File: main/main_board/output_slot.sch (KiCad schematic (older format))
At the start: 6 parts, among them M1 microzed, P1 my_pcie_8x

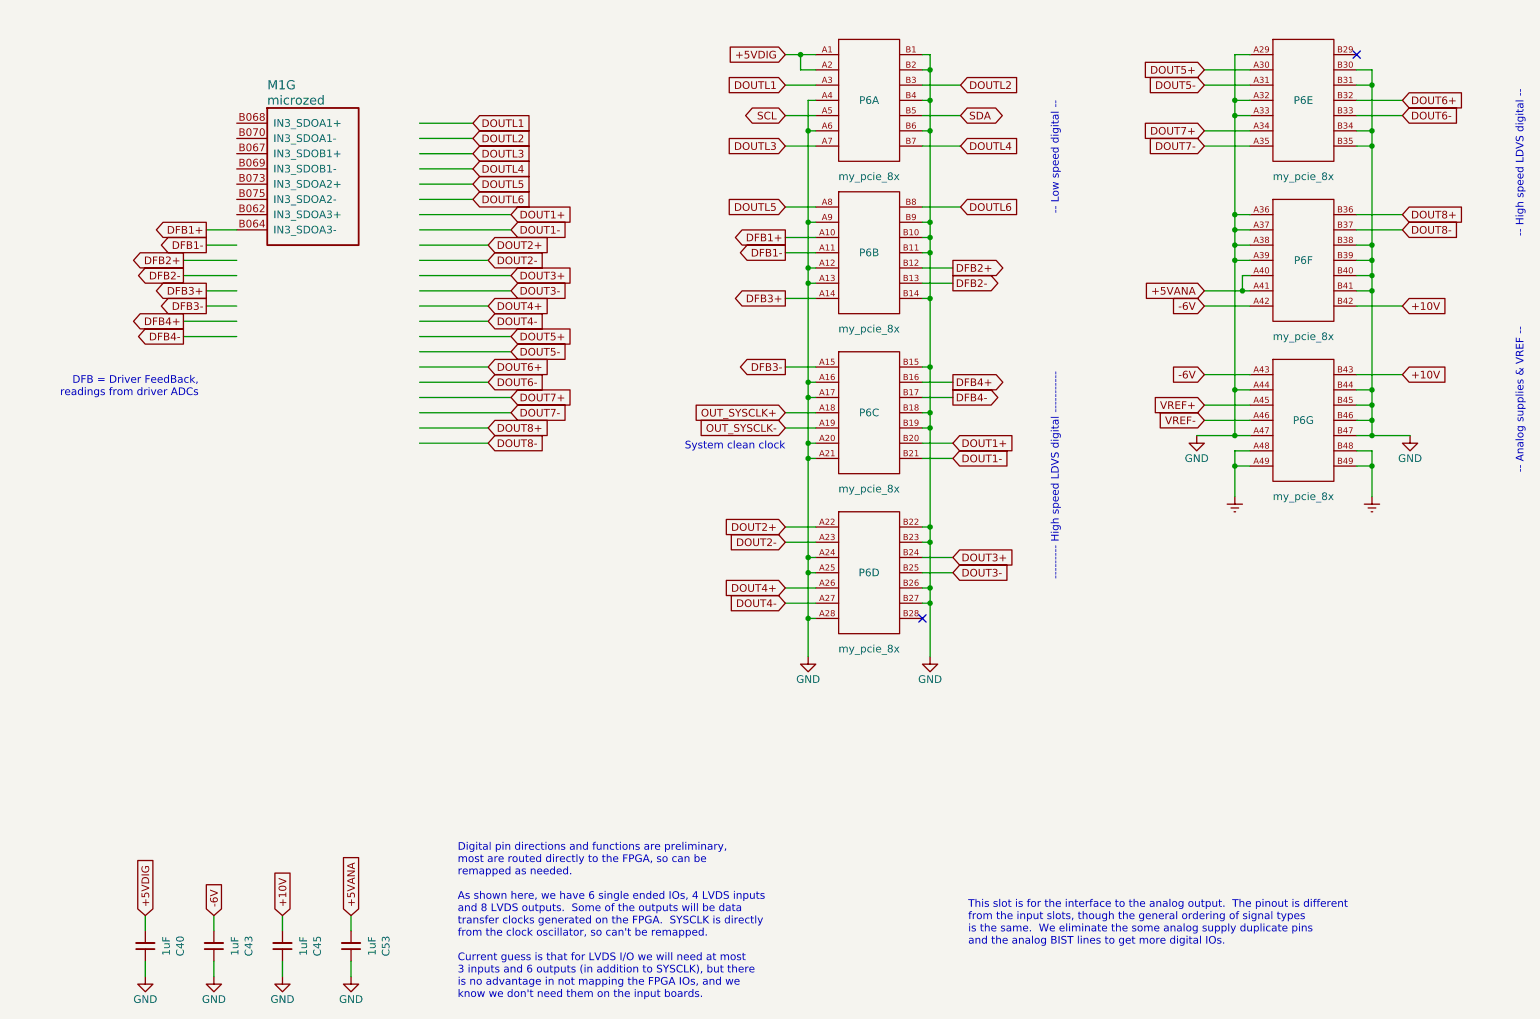
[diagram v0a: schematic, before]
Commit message: Various preparations for routing the main board. Cleaned up the BOM and reconciled it with the Digikey BOM, so lots of component attributes have changed. This involved pinning down some components which had been vague, especially ferrite beads and chip capacitors. 1uF capacitors have all been changed to 10uF. Changed CARDSEL lines to be buffered rather than filtered, since we had the unused buffers sitting there. Another pass on the Microzed pin mapping.  Brought out the DEBUG LVDS line, and tweaked orderings. Added RC filter and pullups on I2C and PROBE_CONFIG.  We might need level translators here to get >=3.3V Added mount holes for the low volt regulator daughtercard, and dimensioned the connector location.
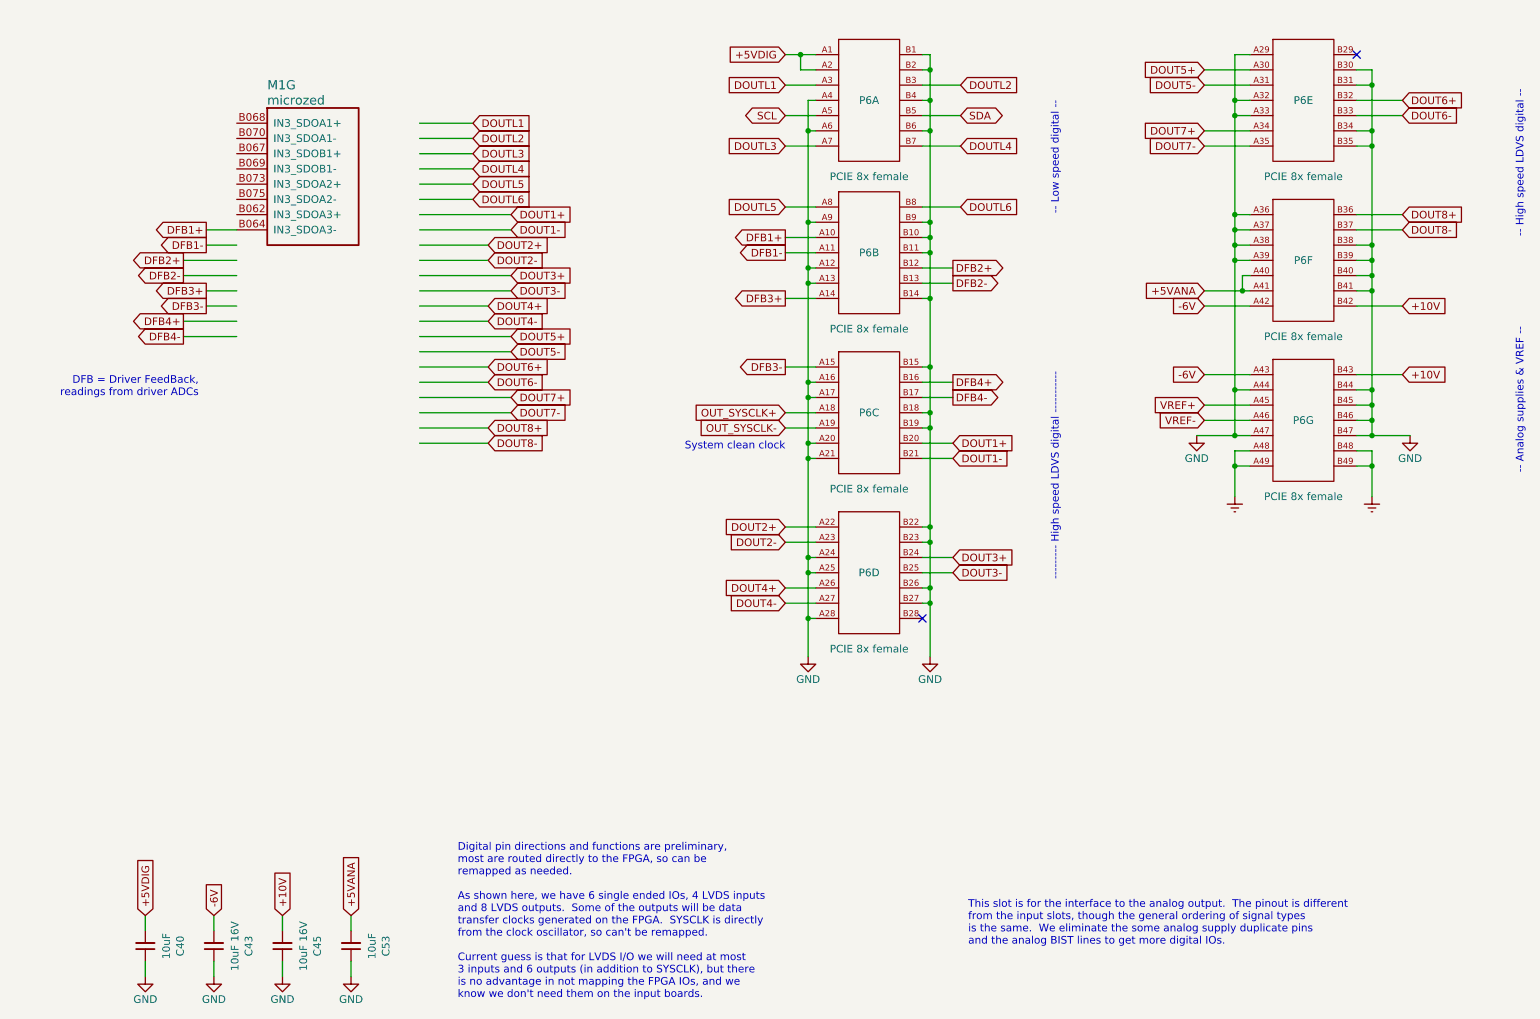
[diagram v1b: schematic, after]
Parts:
- C40, C53: value 1uF -> 10uF; footprint Capacitor_SMD:C_0805_2012Metric -> Capacitor_SMD:C_0603_1608Metric; DK line 27 -> 20; Description CAP CER 1UF 16V X7R 0805 -> CAP CER 10UF 6.3V X5R 0603; Digikey 1276-6471-1-ND -> 478-5318-1-ND; MPN CL21B105KOFNNNG -> 06036D106MAT2A; Manufacturer (none) -> AVX
- C43, C45: value 1uF -> 10uF 16V; DK line 27 -> 10; Description CAP CER 1UF 16V X7R 0805 -> CAP CER 10UF 16V X5R 0805; Digikey 1276-6471-1-ND -> 399-8012-1-ND; MPN CL21B105KOFNNNG -> C0805C106K4PACTU; Manufacturer (none) -> KEMET
- P1: value my_pcie_8x -> PCIE 8x female; DK line (none) -> 2; Description (none) -> CONN PCI EXP FEMALE 98POS 0.039; Digikey (none) -> 609-1970-ND; MPN (none) -> 10018783-10102TLF; Manufacturer (none) -> Amphenol ICC (FCI)
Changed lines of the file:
@@
 AR Path="/5EC15224/5EC152AD" Ref="P6"  Part="3"
 F 0 "P6" H 6450 3450 50  0000 C CNN
-F 1 "my_pcie_8x" H 6450 2950 50  0000 C CNN
+F 1 "PCIE 8x female" H 6450 2950 50  0000 C CNN
 F 2 "input:PCIE_8x_female" H 6450 3950 50  0001 C CNN
-F 3 "" H 6450 3450 50  0001 C CNN
+F 3 "https://www.amphenol-icc.com/media/wysiwyg/files/drawing/10018783.pdf" H 6450 3450 50  0001 C CNN
+F 4 "CONN PCI EXP FEMALE 98POS 0.039" H 6450 3450 50  0001 C CNN "Description"
+F 5 "609-1970-ND" H 6450 3450 50  0001 C CNN "Digikey"
+F 6 "10018783-10102TLF" H 6450 3450 50  0001 C CNN "MPN"
+F 7 "Amphenol ICC (FCI)" H 6450 3450 50  0001 C CNN "Manufacturer"
+F 8 "2" H 6450 3450 50  0001 C CNN "DK line"
 	3    6450 3450
 	1    0    0    -1
@@
 AR Path="/5EC15224/5EC152AF" Ref="P6"  Part="5"
 F 0 "P6" H 9300 1400 50  0000 C CNN
-F 1 "my_pcie_8x" H 9300 900 50  0000 C CNN
+F 1 "PCIE 8x female" H 9300 900 50  0000 C CNN
 F 2 "input:PCIE_8x_female" H 9300 1900 50  0001 C CNN
-F 3 "" H 9300 1400 50  0001 C CNN
+F 3 "https://www.amphenol-icc.com/media/wysiwyg/files/drawing/10018783.pdf" H 9300 1400 50  0001 C CNN
+F 4 "CONN PCI EXP FEMALE 98POS 0.039" H 9300 1400 50  0001 C CNN "Description"
+F 5 "609-1970-ND" H 9300 1400 50  0001 C CNN "Digikey"
+F 6 "10018783-10102TLF" H 9300 1400 50  0001 C CNN "MPN"
+F 7 "Amphenol ICC (FCI)" H 9300 1400 50  0001 C CNN "Manufacturer"
+F 8 "2" H 9300 1400 50  0001 C CNN "DK line"
 	5    9300 1400
 	1    0    0    -1
@@
 AR Path="/5EC15224/5EC152A8" Ref="P6"  Part="6"
 F 0 "P6" H 9300 2450 50  0000 C CNN
-F 1 "my_pcie_8x" H 9300 1950 50  0000 C CNN
+F 1 "PCIE 8x female" H 9300 1950 50  0000 C CNN
 F 2 "input:PCIE_8x_female" H 9300 2950 50  0001 C CNN
-F 3 "" H 9300 2450 50  0001 C CNN
+F 3 "https://www.amphenol-icc.com/media/wysiwyg/files/drawing/10018783.pdf" H 9300 2450 50  0001 C CNN
+F 4 "CONN PCI EXP FEMALE 98POS 0.039" H 9300 2450 50  0001 C CNN "Description"
+F 5 "609-1970-ND" H 9300 2450 50  0001 C CNN "Digikey"
+F 6 "10018783-10102TLF" H 9300 2450 50  0001 C CNN "MPN"
+F 7 "Amphenol ICC (FCI)" H 9300 2450 50  0001 C CNN "Manufacturer"
+F 8 "2" H 9300 2450 50  0001 C CNN "DK line"
 	6    9300 2450
 	1    0    0    -1
@@
 AR Path="/5EC15224/5EC152A9" Ref="P6"  Part="7"
 F 0 "P6" H 9300 3500 50  0000 C CNN
-F 1 "my_pcie_8x" H 9300 3000 50  0000 C CNN
+F 1 "PCIE 8x female" H 9300 3000 50  0000 C CNN
 F 2 "input:PCIE_8x_female" H 9300 4000 50  0001 C CNN
-F 3 "" H 9300 3500 50  0001 C CNN
+F 3 "https://www.amphenol-icc.com/media/wysiwyg/files/drawing/10018783.pdf" H 9300 3500 50  0001 C CNN
+F 4 "CONN PCI EXP FEMALE 98POS 0.039" H 9300 3500 50  0001 C CNN "Description"
+F 5 "609-1970-ND" H 9300 3500 50  0001 C CNN "Digikey"
+F 6 "10018783-10102TLF" H 9300 3500 50  0001 C CNN "MPN"
+F 7 "Amphenol ICC (FCI)" H 9300 3500 50  0001 C CNN "Manufacturer"
+F 8 "2" H 9300 3500 50  0001 C CNN "DK line"
 	7    9300 3500
 	1    0    0    -1
@@
 AR Path="/5EC15224/5E625DE3" Ref="P6"  Part="2"
 F 0 "P6" H 6450 2400 50  0000 C CNN
-F 1 "my_pcie_8x" H 6450 1900 50  0000 C CNN
+F 1 "PCIE 8x female" H 6450 1900 50  0000 C CNN
 F 2 "input:PCIE_8x_female" H 6450 2900 50  0001 C CNN
-F 3 "" H 6450 2400 50  0001 C CNN
+F 3 "https://www.amphenol-icc.com/media/wysiwyg/files/drawing/10018783.pdf" H 6450 2400 50  0001 C CNN
+F 4 "CONN PCI EXP FEMALE 98POS 0.039" H 6450 2400 50  0001 C CNN "Description"
+F 5 "609-1970-ND" H 6450 2400 50  0001 C CNN "Digikey"
+F 6 "10018783-10102TLF" H 6450 2400 50  0001 C CNN "MPN"
+F 7 "Amphenol ICC (FCI)" H 6450 2400 50  0001 C CNN "Manufacturer"
+F 8 "2" H 6450 2400 50  0001 C CNN "DK line"
 	2    6450 2400
 	1    0    0    -1
@@
 AR Path="/5EC15224/5EC152AE" Ref="P6"  Part="1"
 F 0 "P6" H 6450 1400 50  0000 C CNN
-F 1 "my_pcie_8x" H 6450 900 50  0000 C CNN
+F 1 "PCIE 8x female" H 6450 900 50  0000 C CNN
 F 2 "input:PCIE_8x_female" H 6450 1900 50  0001 C CNN
-F 3 "" H 6450 1400 50  0001 C CNN
+F 3 "https://www.amphenol-icc.com/media/wysiwyg/files/drawing/10018783.pdf" H 6450 1400 50  0001 C CNN
+F 4 "CONN PCI EXP FEMALE 98POS 0.039" H 6450 1400 50  0001 C CNN "Description"
+F 5 "609-1970-ND" H 6450 1400 50  0001 C CNN "Digikey"
+F 6 "10018783-10102TLF" H 6450 1400 50  0001 C CNN "MPN"
+F 7 "Amphenol ICC (FCI)" H 6450 1400 50  0001 C CNN "Manufacturer"
+F 8 "2" H 6450 1400 50  0001 C CNN "DK line"
 	1    6450 1400
 	1    0    0    -1
@@
 AR Path="/5EC15224/5E625DE5" Ref="P6"  Part="4"
 F 0 "P6" H 6450 4500 50  0000 C CNN
-F 1 "my_pcie_8x" H 6450 4000 50  0000 C CNN
+F 1 "PCIE 8x female" H 6450 4000 50  0000 C CNN
 F 2 "input:PCIE_8x_female" H 6450 5000 50  0001 C CNN
-F 3 "" H 6450 4500 50  0001 C CNN
+F 3 "https://www.amphenol-icc.com/media/wysiwyg/files/drawing/10018783.pdf" H 6450 4500 50  0001 C CNN
+F 4 "CONN PCI EXP FEMALE 98POS 0.039" H 6450 4500 50  0001 C CNN "Description"
+F 5 "609-1970-ND" H 6450 4500 50  0001 C CNN "Digikey"
+F 6 "10018783-10102TLF" H 6450 4500 50  0001 C CNN "MPN"
+F 7 "Amphenol ICC (FCI)" H 6450 4500 50  0001 C CNN "Manufacturer"
+F 8 "2" H 6450 4500 50  0001 C CNN "DK line"
 	4    6450 4500
 	1    0    0    -1
@@
 AR Path="/5EC15224/5EE014BD" Ref="C40"  Part="1"
 F 0 "C40" V 1471 6950 50  0000 C CNN
-F 1 "1uF" V 1562 6950 50  0000 C CNN
-F 2 "Capacitor_SMD:C_0805_2012Metric" H 1700 6950 50  0001 C CNN
-F 3 "https://media.digikey.com/pdf/Data%20Sheets/Samsung%20PDFs/CL_Series_MLCC_ds.pdf" H 1700 6950 50  0001 C CNN
-F 4 "CAP CER 1UF 16V X7R 0805 " H 1700 6950 50  0001 C CNN "Description"
-F 5 "1276-6471-1-ND" H 1700 6950 50  0001 C CNN "Digikey"
-F 6 "CL21B105KOFNNNG" H 1700 6950 50  0001 C CNN "MPN"
-F 7 "27" H 1700 6950 50  0001 C CNN "DK line"
+F 1 "10uF" V 1562 6950 50  0000 C CNN
+F 2 "Capacitor_SMD:C_0603_1608Metric" H 1700 6950 50  0001 C CNN
+F 3 "http://datasheets.avx.com/cx5r.pdf" H 1700 6950 50  0001 C CNN
+F 4 "CAP CER 10UF 6.3V X5R 0603" H 1700 6950 50  0001 C CNN "Description"
+F 5 "478-5318-1-ND" H 1700 6950 50  0001 C CNN "Digikey"
+F 6 "06036D106MAT2A" H 1700 6950 50  0001 C CNN "MPN"
+F 7 "20" H 1700 6950 50  0001 C CNN "DK line"
+F 8 "AVX" H 1700 6950 50  0001 C CNN "Manufacturer"
 	1    1700 6950
 	-1   0    0    1
@@
 AR Path="/5EC15224/5EE014CF" Ref="C43"  Part="1"
 F 0 "C43" V 1921 6950 50  0000 C CNN
-F 1 "1uF" V 2012 6950 50  0000 C CNN
+F 1 "10uF 16V" V 2012 6950 50  0000 C CNN
 F 2 "Capacitor_SMD:C_0805_2012Metric" H 2150 6950 50  0001 C CNN
-F 3 "https://media.digikey.com/pdf/Data%20Sheets/Samsung%20PDFs/CL_Series_MLCC_ds.pdf" H 2150 6950 50  0001 C CNN
-F 4 "CAP CER 1UF 16V X7R 0805 " H 2150 6950 50  0001 C CNN "Description"
-F 5 "1276-6471-1-ND" H 2150 6950 50  0001 C CNN "Digikey"
-F 6 "CL21B105KOFNNNG" H 2150 6950 50  0001 C CNN "MPN"
-F 7 "27" H 2150 6950 50  0001 C CNN "DK line"
+F 3 "https://api.kemet.com/component-edge/download/datasheet/C0805C106K4PACTU.pdf" H 2150 6950 50  0001 C CNN
+F 4 "CAP CER 10UF 16V X5R 0805" H 2150 6950 50  0001 C CNN "Description"
+F 5 "399-8012-1-ND" H 2150 6950 50  0001 C CNN "Digikey"
+F 6 "C0805C106K4PACTU" H 2150 6950 50  0001 C CNN "MPN"
+F 7 "10" H 2150 6950 50  0001 C CNN "DK line"
+F 8 "" H 2150 6950 50  0001 C CNN "MFG"
+F 9 "KEMET" H 2150 6950 50  0001 C CNN "Manufacturer"
 	1    2150 6950
 	-1   0    0    1
@@
 AR Path="/5EC15224/5EE014E1" Ref="C45"  Part="1"
 F 0 "C45" V 2371 6950 50  0000 C CNN
-F 1 "1uF" V 2462 6950 50  0000 C CNN
+F 1 "10uF 16V" V 2462 6950 50  0000 C CNN
 F 2 "Capacitor_SMD:C_0805_2012Metric" H 2600 6950 50  0001 C CNN
-F 3 "https://media.digikey.com/pdf/Data%20Sheets/Samsung%20PDFs/CL_Series_MLCC_ds.pdf" H 2600 6950 50  0001 C CNN
-F 4 "CAP CER 1UF 16V X7R 0805 " H 2600 6950 50  0001 C CNN "Description"
-F 5 "1276-6471-1-ND" H 2600 6950 50  0001 C CNN "Digikey"
-F 6 "CL21B105KOFNNNG" H 2600 6950 50  0001 C CNN "MPN"
-F 7 "27" H 2600 6950 50  0001 C CNN "DK line"
+F 3 "https://api.kemet.com/component-edge/download/datasheet/C0805C106K4PACTU.pdf" H 2600 6950 50  0001 C CNN
+F 4 "CAP CER 10UF 16V X5R 0805" H 2600 6950 50  0001 C CNN "Description"
+F 5 "399-8012-1-ND" H 2600 6950 50  0001 C CNN "Digikey"
+F 6 "C0805C106K4PACTU" H 2600 6950 50  0001 C CNN "MPN"
+F 7 "10" H 2600 6950 50  0001 C CNN "DK line"
+F 8 "" H 2600 6950 50  0001 C CNN "MFG"
+F 9 "KEMET" H 2600 6950 50  0001 C CNN "Manufacturer"
 	1    2600 6950
 	-1   0    0    1
@@
 AR Path="/5EC15224/5EE014F3" Ref="C53"  Part="1"
 F 0 "C53" V 2821 6950 50  0000 C CNN
-F 1 "1uF" V 2912 6950 50  0000 C CNN
-F 2 "Capacitor_SMD:C_0805_2012Metric" H 3050 6950 50  0001 C CNN
-F 3 "https://media.digikey.com/pdf/Data%20Sheets/Samsung%20PDFs/CL_Series_MLCC_ds.pdf" H 3050 6950 50  0001 C CNN
-F 4 "CAP CER 1UF 16V X7R 0805 " H 3050 6950 50  0001 C CNN "Description"
-F 5 "1276-6471-1-ND" H 3050 6950 50  0001 C CNN "Digikey"
-F 6 "CL21B105KOFNNNG" H 3050 6950 50  0001 C CNN "MPN"
-F 7 "27" H 3050 6950 50  0001 C CNN "DK line"
+F 1 "10uF" V 2912 6950 50  0000 C CNN
+F 2 "Capacitor_SMD:C_0603_1608Metric" H 3050 6950 50  0001 C CNN
+F 3 "http://datasheets.avx.com/cx5r.pdf" H 3050 6950 50  0001 C CNN
+F 4 "CAP CER 10UF 6.3V X5R 0603" H 3050 6950 50  0001 C CNN "Description"
+F 5 "478-5318-1-ND" H 3050 6950 50  0001 C CNN "Digikey"
+F 6 "06036D106MAT2A" H 3050 6950 50  0001 C CNN "MPN"
+F 7 "20" H 3050 6950 50  0001 C CNN "DK line"
+F 8 "AVX" H 3050 6950 50  0001 C CNN "Manufacturer"
 	1    3050 6950
 	-1   0    0    1

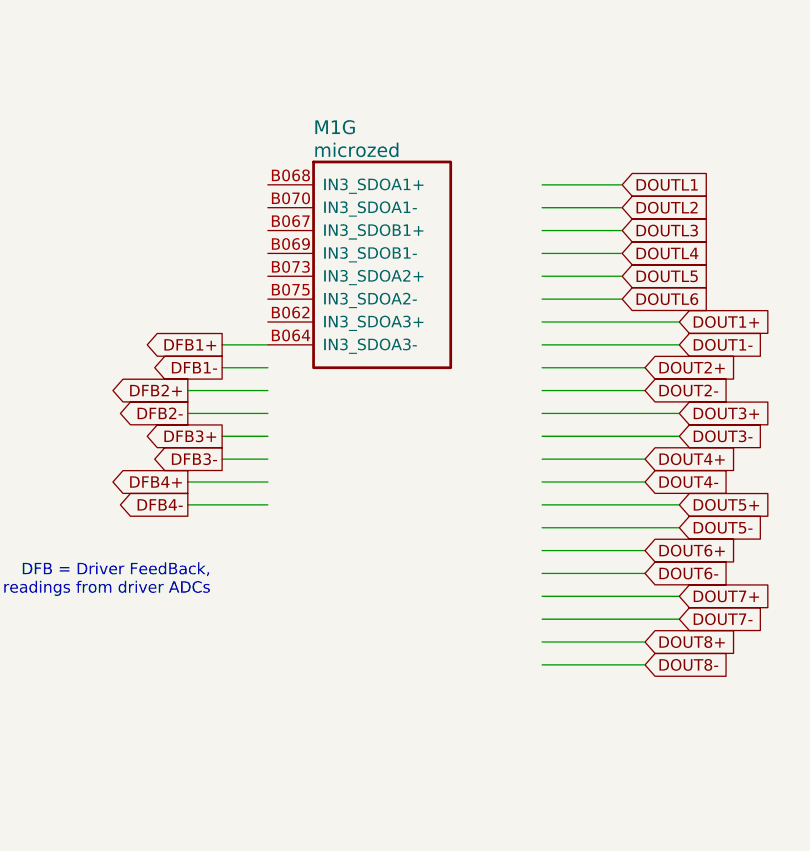
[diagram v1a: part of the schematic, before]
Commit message: Added testpoints, debug IO port, LEDs, and clock output jack.
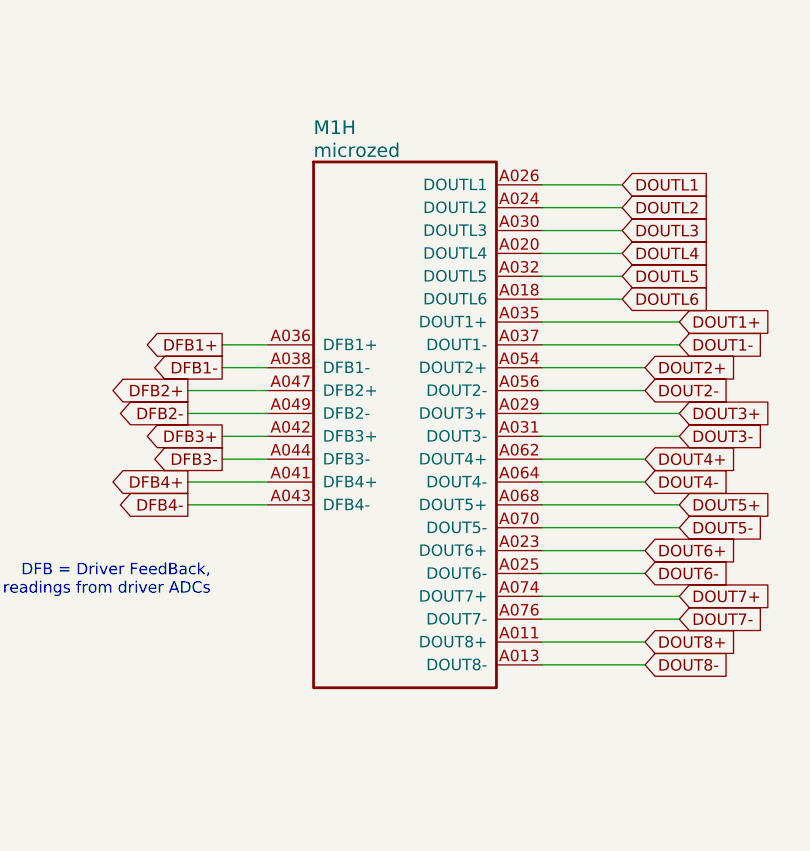
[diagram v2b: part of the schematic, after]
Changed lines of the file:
@@
 $Comp
 L microzed:microzed M1
-U 7 1 5F1DB65F
+U 8 1 5F1DB65F
 P 2300 1550
 F 0 "M1" H 2500 1800 60  0000 L CNN
@@
 F 2 "main_board:Microzed" H 2500 1600 60  0001 L CNN
 F 3 "" H 2500 1400 60  0001 L CNN
-	7    2300 1550
+	8    2300 1550
 	1    0    0    -1
 $EndComp
